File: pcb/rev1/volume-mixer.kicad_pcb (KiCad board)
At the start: 4 copper layers, 120 x 150 mm, 172 parts, among them CON1 TC2030-IDC, J1 Conn_01x04_Pin, J10 Conn_01x04_Pin, J2 Conn_01x10_Pin, J3 Conn_01x10_Pin, J4 Conn_01x04_Pin, J5 JST, J6 Conn_01x04_Pin, J7 Conn_01x04_Pin, J8 Conn_01x04_Pin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

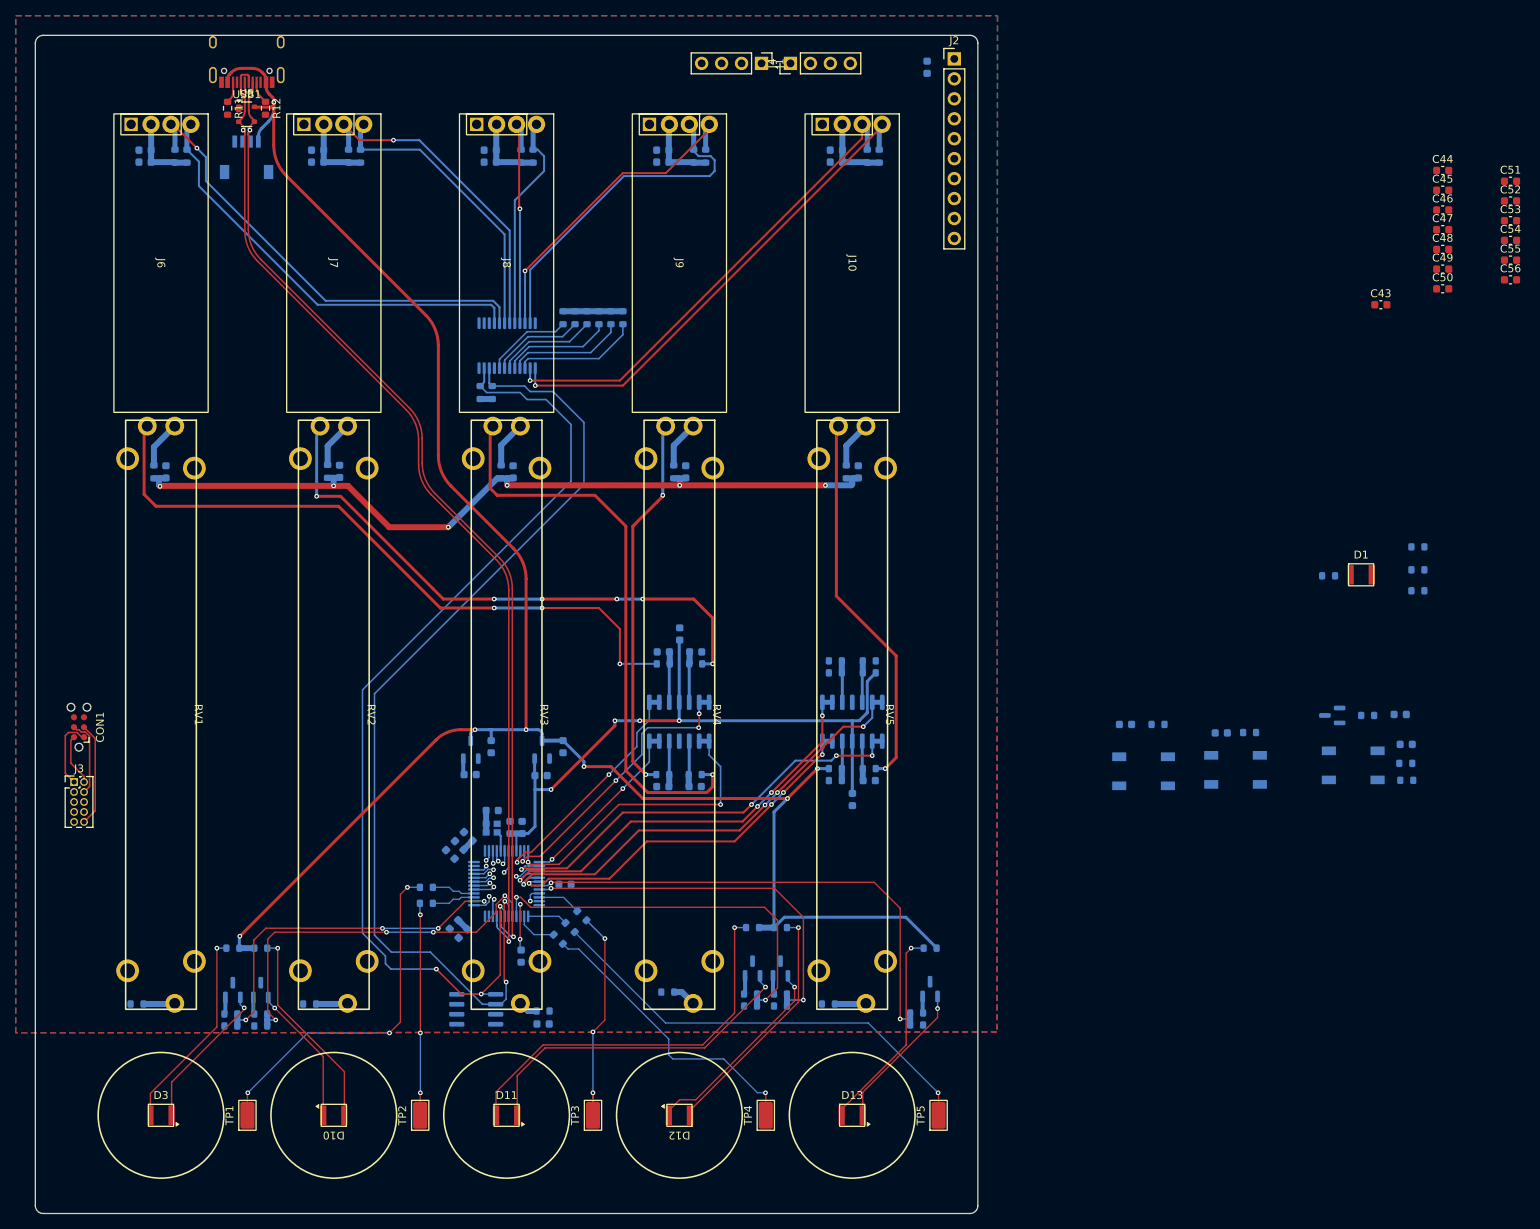
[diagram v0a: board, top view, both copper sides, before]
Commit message: Added config file and corrected build issues
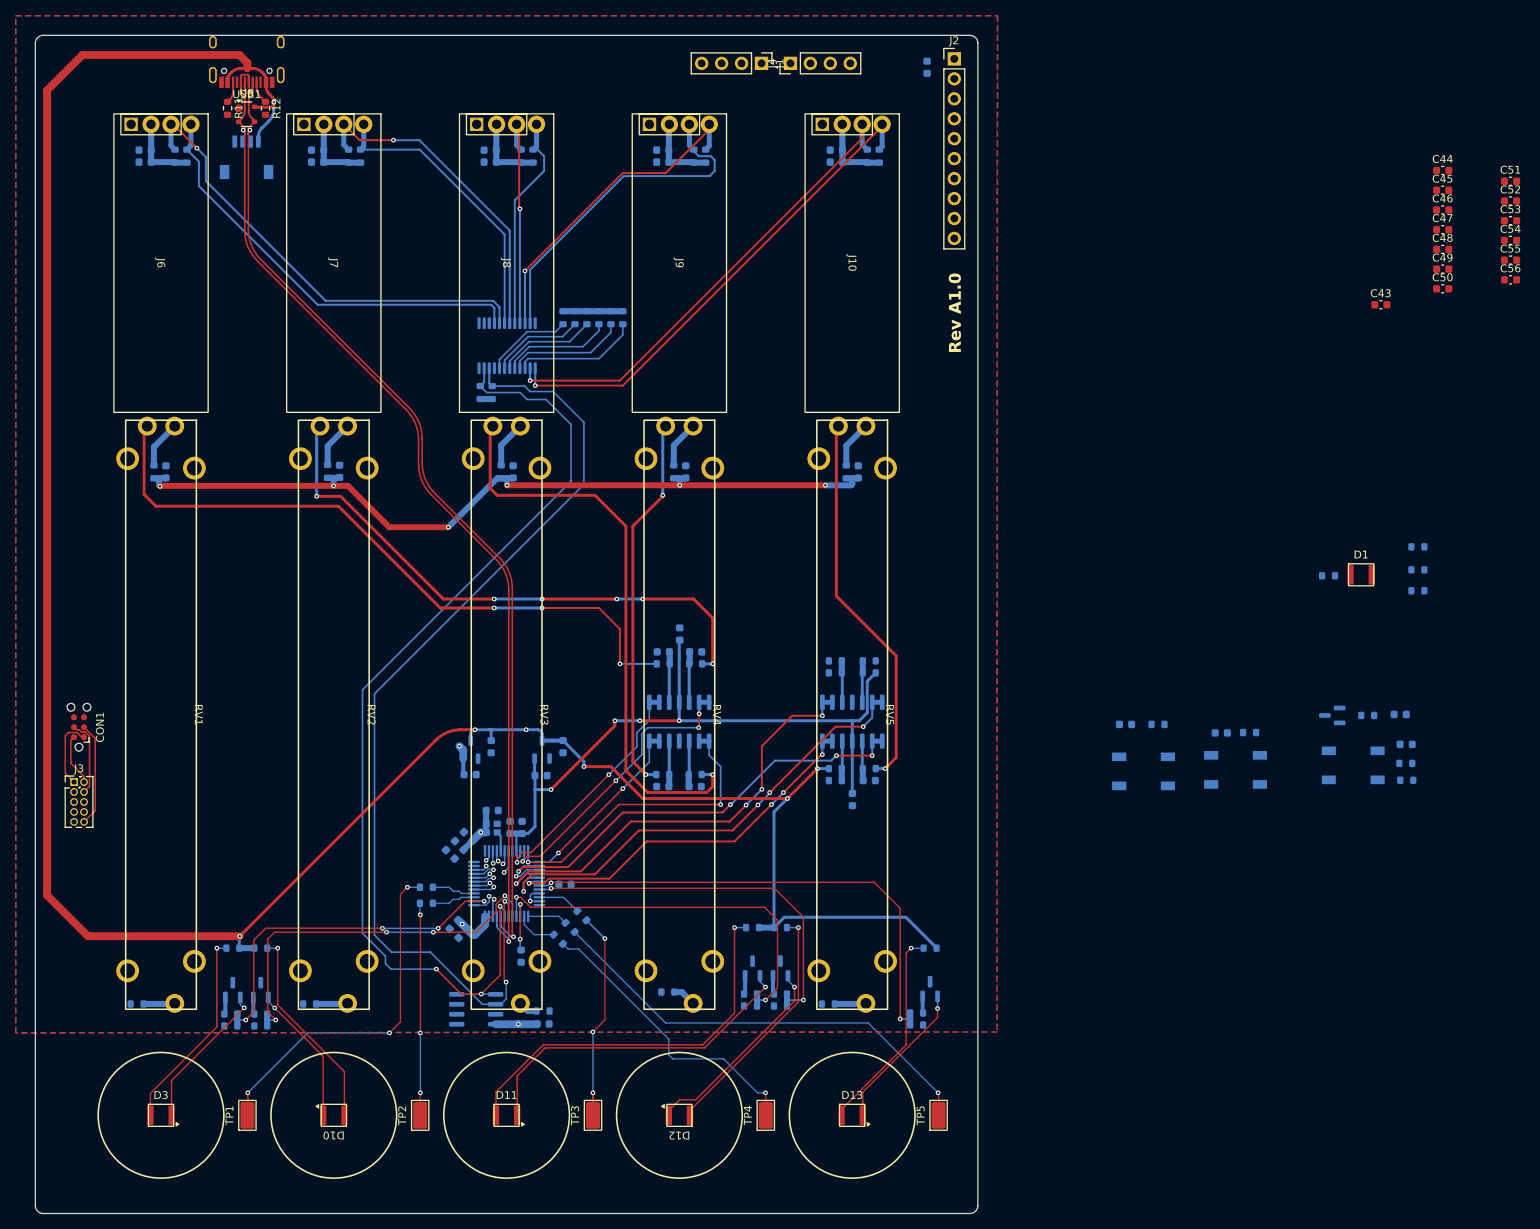
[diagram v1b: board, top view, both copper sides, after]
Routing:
- net VBUS: track 251.1 -> 316.8 mm
- net +3V3: track 74.0 -> 134.8 mm, vias 0 -> 4
- net Vref digi: track 54.9 -> 57.5 mm
- net Vref ana: track 59.0 -> 60.8 mm
- net Slider4: track 56.4 -> 57.3 mm
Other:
- board text added: "Rev A1.0"
